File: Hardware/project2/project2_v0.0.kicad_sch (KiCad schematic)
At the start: 17 parts, among them J1 Conn_01x02, J3 Conn_01x02, J5 Conn_01x03, J6 Conn_01x02, Q1 Q_NMOS_GSD

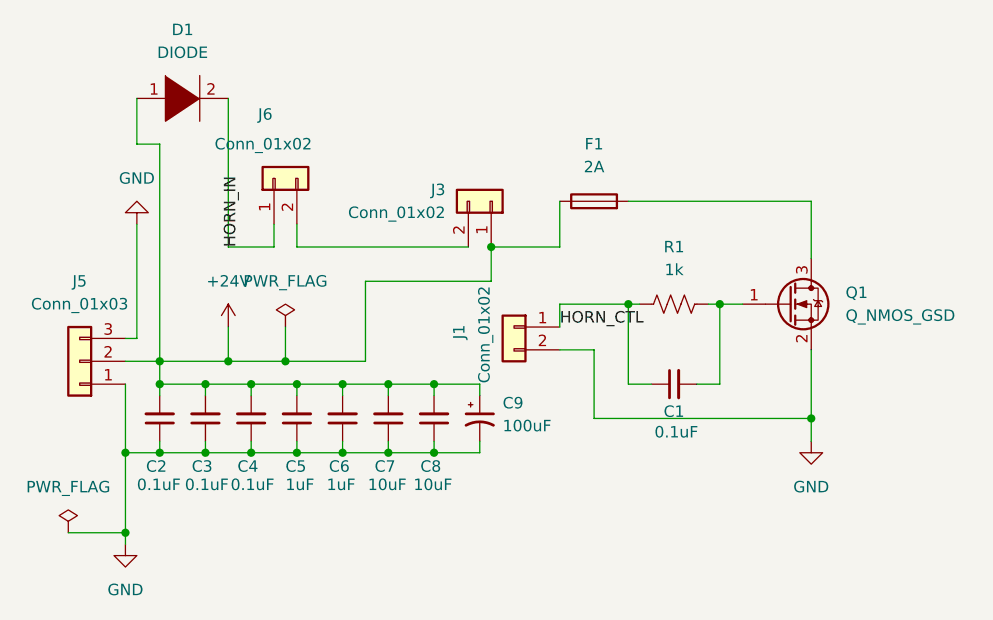
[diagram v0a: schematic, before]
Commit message: finished layout and Instant DFM Report
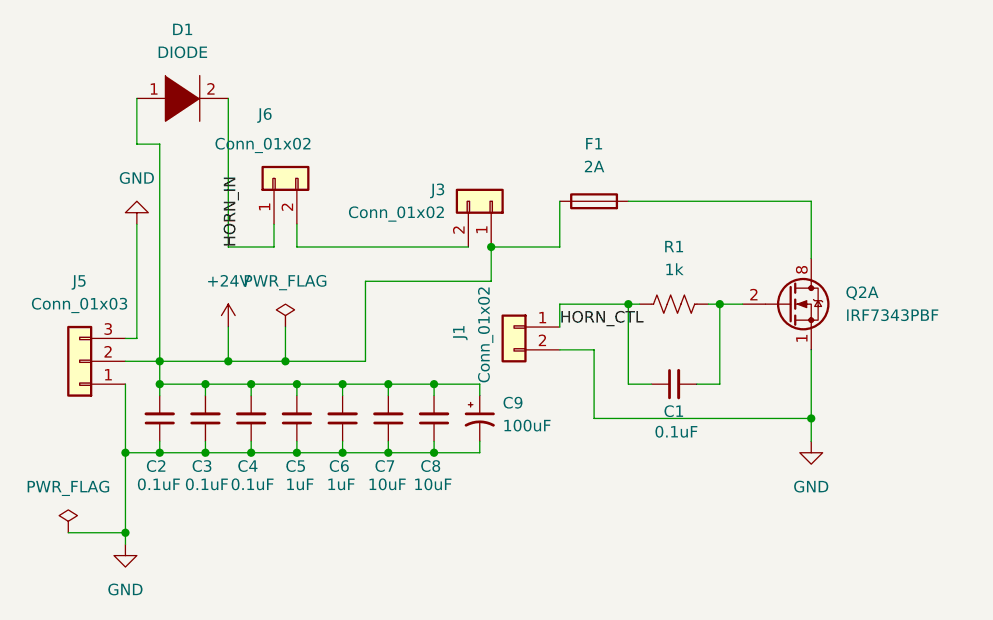
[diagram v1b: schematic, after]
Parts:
- removed Q1: Q_NMOS_GSD, symbol Device:Q_NMOS_GSD
- added Q2: IRF7343PBF, Package_SO:SOIC-8_3.9x4.9mm_P1.27mm, symbol Transistor_FET:IRF7343PBF
- C1, C2, C3, C4, C5, C6: footprint (none) -> Capacitor_SMD:C_0603_1608Metric
- C7, C8: footprint (none) -> Capacitor_SMD:C_1206_3216Metric
- C9: footprint (none) -> Capacitor_THT:C_Radial_D10.0mm_H20.0mm_P5.00mm
- D1: footprint (none) -> Diode_SMD:D_SMA
- F1: footprint (none) -> Fuse:Fuse_0402_1005Metric
- J1, J3, J6: footprint (none) -> Connector_Molex:Molex_KK-254_AE-6410-02A_1x02_P2.54mm_Vertical
- J5: footprint (none) -> Connector_Molex:Molex_KK-396_5273-03A_1x03_P3.96mm_Vertical
- R1: footprint (none) -> Resistor_SMD:R_0603_1608Metric_Pad0.98x0.95mm_HandSolder
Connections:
- net GND: now also Q2.1 (S)
- net at C1.2, R1.2: now also Q2.2 (G)
- net at F1.2: now also Q2.7 (D), Q2.8 (D)
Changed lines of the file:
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@@
 			)
 		)
-		(property "Footprint" ""
+		(property "Footprint" "Capacitor_SMD:C_1206_3216Metric"
 			(at 107.95 91.44 0)
 			(effects
@@
 			)
 		)
-		(property "Footprint" ""
+		(property "Footprint" "Connector_Molex:Molex_KK-396_5273-03A_1x03_P3.96mm_Vertical"
 			(at 73.66 85.09 0)
 			(effects
@@
 			)
 		)
-		(property "Footprint" ""
+		(property "Footprint" "Resistor_SMD:R_0603_1608Metric_Pad0.98x0.95mm_HandSolder"
 			(at 139.954 77.724 90)
 			(effects
@@
 				(path "/1e1b062d-fad0-427c-a622-c5b8a80b5268"
 					(reference "R1")
+					(unit 1)
+				)
+			)
+		)
+	)
+	(symbol
+		(lib_id "Transistor_FET:IRF7343PBF")
+		(at 152.4 78.74 0)
+		(unit 1)
+		(exclude_from_sim no)
+		(in_bom yes)
+		(on_board yes)
+		(dnp no)
+		(fields_autoplaced yes)
+		(property "Reference" "Q2"
+			(at 158.75 77.4699 0)
+			(effects
+				(font
+					(size 1.27 1.27)
+				)
+				(justify left)
+			)
+		)
+		(property "Value" "IRF7343PBF"
+			(at 158.75 80.0099 0)
+			(effects
+				(font
+					(size 1.27 1.27)
+				)
+				(justify left)
+			)
+		)
+		(property "Footprint" "Package_SO:SOIC-8_3.9x4.9mm_P1.27mm"
+			(at 157.48 80.645 0)
+			(effects
+				(font
+					(size 1.27 1.27)
+				)
+				(justify left)
+				(hide yes)
+			)
+		)
+		(property "Datasheet" "http://www.irf.com/product-info/datasheets/data/irf7343ipbf.pdf"
+			(at 154.94 78.74 0)
+			(effects
+				(font
+					(size 1.27 1.27)
+				)
+				(justify left)
+				(hide yes)
+			)
+		)
+		(property "Description" "4A Id, 55V Vds, Dual HEXFET MOSFET, SO-8"
+			(at 152.4 78.74 0)
+			(effects
+				(font
+					(size 1.27 1.27)
+				)
+				(hide yes)
+			)
+		)
+		(pin "6"
+		)
+		(pin "3"
+		)
+		(pin "5"
+		)
+		(pin "7"
+		)
+		(pin "8"
+		)
+		(pin "2"
+		)
+		(pin "1"
+		)
+		(pin "4"
+		)
+		(instances
+			(project ""
+				(path "/1e1b062d-fad0-427c-a622-c5b8a80b5268"
+					(reference "Q2")
 					(unit 1)
 				)
@@
 			)
 		)
-		(property "Footprint" ""
+		(property "Footprint" "Fuse:Fuse_0402_1005Metric"
 			(at 130.81 69.088 90)
 			(effects
@@
 			)
 		)
-		(property "Footprint" ""
+		(property "Footprint" "Capacitor_SMD:C_0603_1608Metric"
 			(at 97.79 91.44 0)
 			(effects
@@
 			)
 		)
-		(property "Footprint" ""
+		(property "Footprint" "Connector_Molex:Molex_KK-254_AE-6410-02A_1x02_P2.54mm_Vertical"
 			(at 119.38 67.31 0)
 			(effects
@@
 			)
 		)
-		(property "Footprint" ""
+		(property "Footprint" "Capacitor_SMD:C_0603_1608Metric"
 			(at 102.87 91.44 0)
 			(effects
@@
 			)
 		)
-		(property "Footprint" ""
+		(property "Footprint" "Diode_SMD:D_SMA"
 			(at 85.09 55.88 0)
 			(effects
@@
 			)
 		)
-		(property "Footprint" ""
+		(property "Footprint" "Capacitor_SMD:C_0603_1608Metric"
 			(at 87.63 91.44 0)
 			(effects
@@
 			)
 		)
-		(property "Footprint" ""
+		(property "Footprint" "Capacitor_SMD:C_0603_1608Metric"
 			(at 139.7 87.63 0)
 			(effects
@@
 			)
 		)
-		(property "Footprint" ""
+		(property "Footprint" "Capacitor_SMD:C_0603_1608Metric"
 			(at 92.71 91.44 0)
 			(effects
@@
 				(path "/1e1b062d-fad0-427c-a622-c5b8a80b5268"
 					(reference "C4")
-					(unit 1)
-				)
-			)
-		)
-	)
-	(symbol
-		(lib_id "Device:Q_NMOS_GSD")
-		(at 152.4 78.74 0)
-		(unit 1)
-		(exclude_from_sim no)
-		(in_bom yes)
-		(on_board yes)
-		(dnp no)
-		(fields_autoplaced yes)
-		(property "Reference" "Q1"
-			(at 158.75 77.4699 0)
-			(effects
-				(font
-					(size 1.27 1.27)
-				)
-				(justify left)
-			)
-		)
-		(property "Value" "Q_NMOS_GSD"
-			(at 158.75 80.0099 0)
-			(effects
-				(font
-					(size 1.27 1.27)
-				)
-				(justify left)
-			)
-		)
-		(property "Footprint" ""
-			(at 157.48 76.2 0)
-			(effects
-				(font
-					(size 1.27 1.27)
-				)
-				(hide yes)
-			)
-		)
-		(property "Datasheet" "~"
-			(at 152.4 78.74 0)
-			(effects
-				(font
-					(size 1.27 1.27)
-				)
-				(hide yes)
-			)
-		)
-		(property "Description" "N-MOSFET transistor, gate/source/drain"
-			(at 152.4 78.74 0)
-			(effects
-				(font
-					(size 1.27 1.27)
-				)
-				(hide yes)
-			)
-		)
-		(pin "2"
-		)
-		(pin "3"
-		)
-		(pin "1"
-		)
-		(instances
-			(project ""
-				(path "/1e1b062d-fad0-427c-a622-c5b8a80b5268"
-					(reference "Q1")
 					(unit 1)
 				)
@@
 			)
 		)
-		(property "Footprint" ""
+		(property "Footprint" "Capacitor_SMD:C_0603_1608Metric"
 			(at 82.55 91.44 0)
 			(effects
@@
 			)
 		)
-		(property "Footprint" ""
+		(property "Footprint" "Connector_Molex:Molex_KK-254_AE-6410-02A_1x02_P2.54mm_Vertical"
 			(at 95.25 64.77 0)
 			(effects
@@
 			)
 		)
-		(property "Footprint" ""
+		(property "Footprint" "Capacitor_THT:C_Radial_D10.0mm_H20.0mm_P5.00mm"
 			(at 118.11 91.44 0)
 			(effects
@@
 			)
 		)
-		(property "Footprint" ""
+		(property "Footprint" "Connector_Molex:Molex_KK-254_AE-6410-02A_1x02_P2.54mm_Vertical"
 			(at 121.92 81.28 0)
 			(effects
@@
 			)
 		)
-		(property "Footprint" ""
+		(property "Footprint" "Capacitor_SMD:C_1206_3216Metric"
 			(at 113.03 91.44 0)
 			(effects
